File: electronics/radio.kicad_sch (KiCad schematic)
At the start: 33 parts, among them J7 SIM_Card, J9 Conn_Coaxial_Small, Q1 Q_NMOS_GSD, SW1 SW_Push, U2 TPS22953

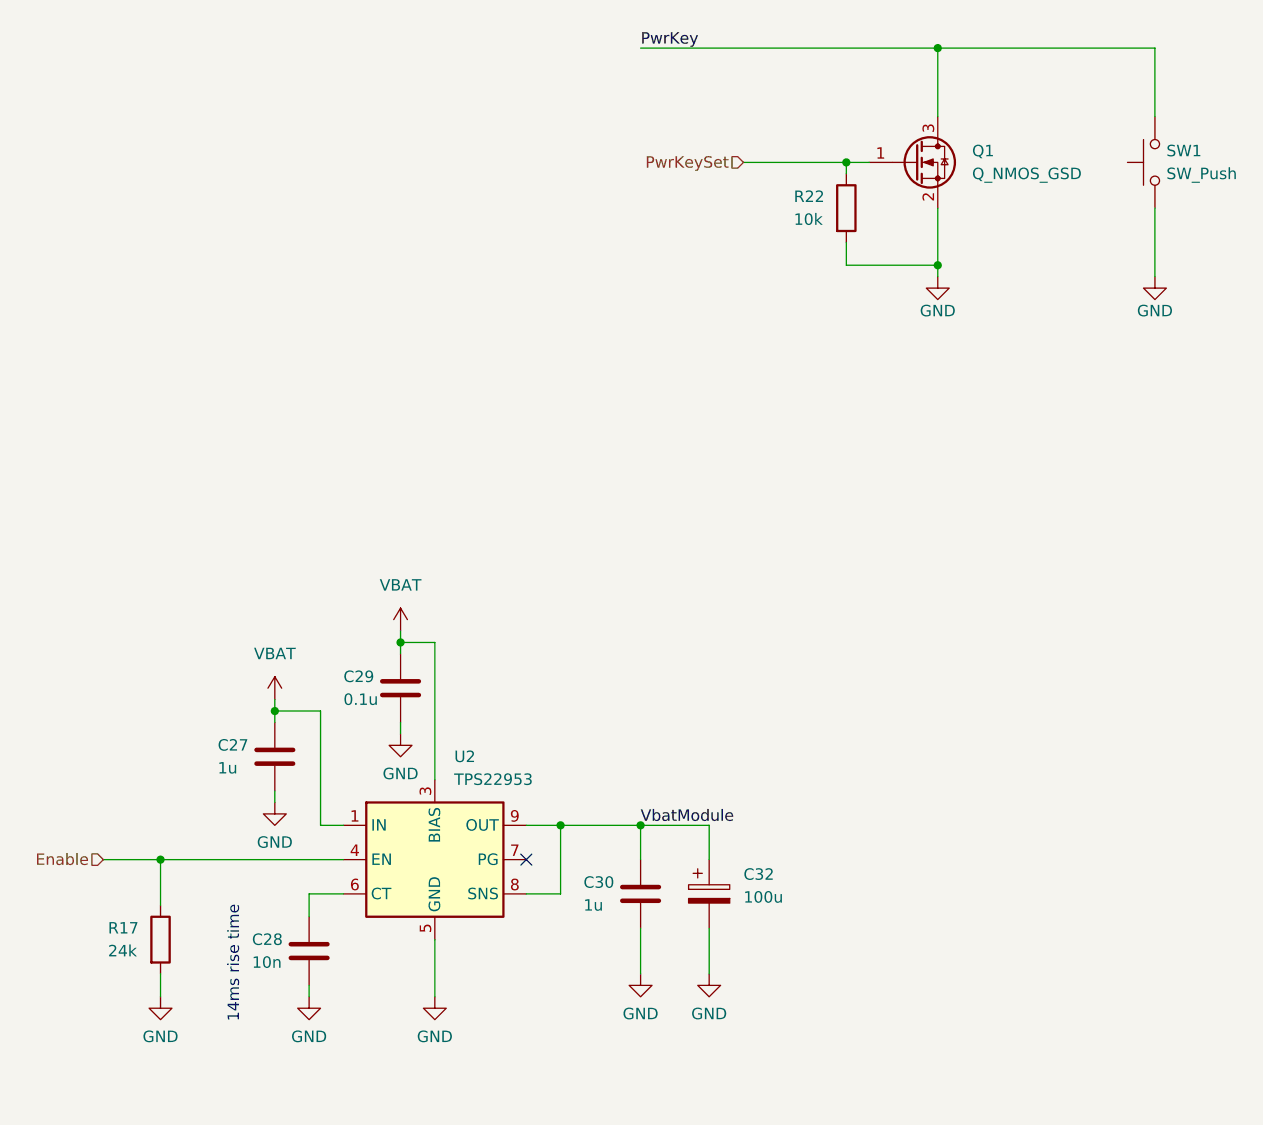
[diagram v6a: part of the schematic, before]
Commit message: electronics: add MPNs
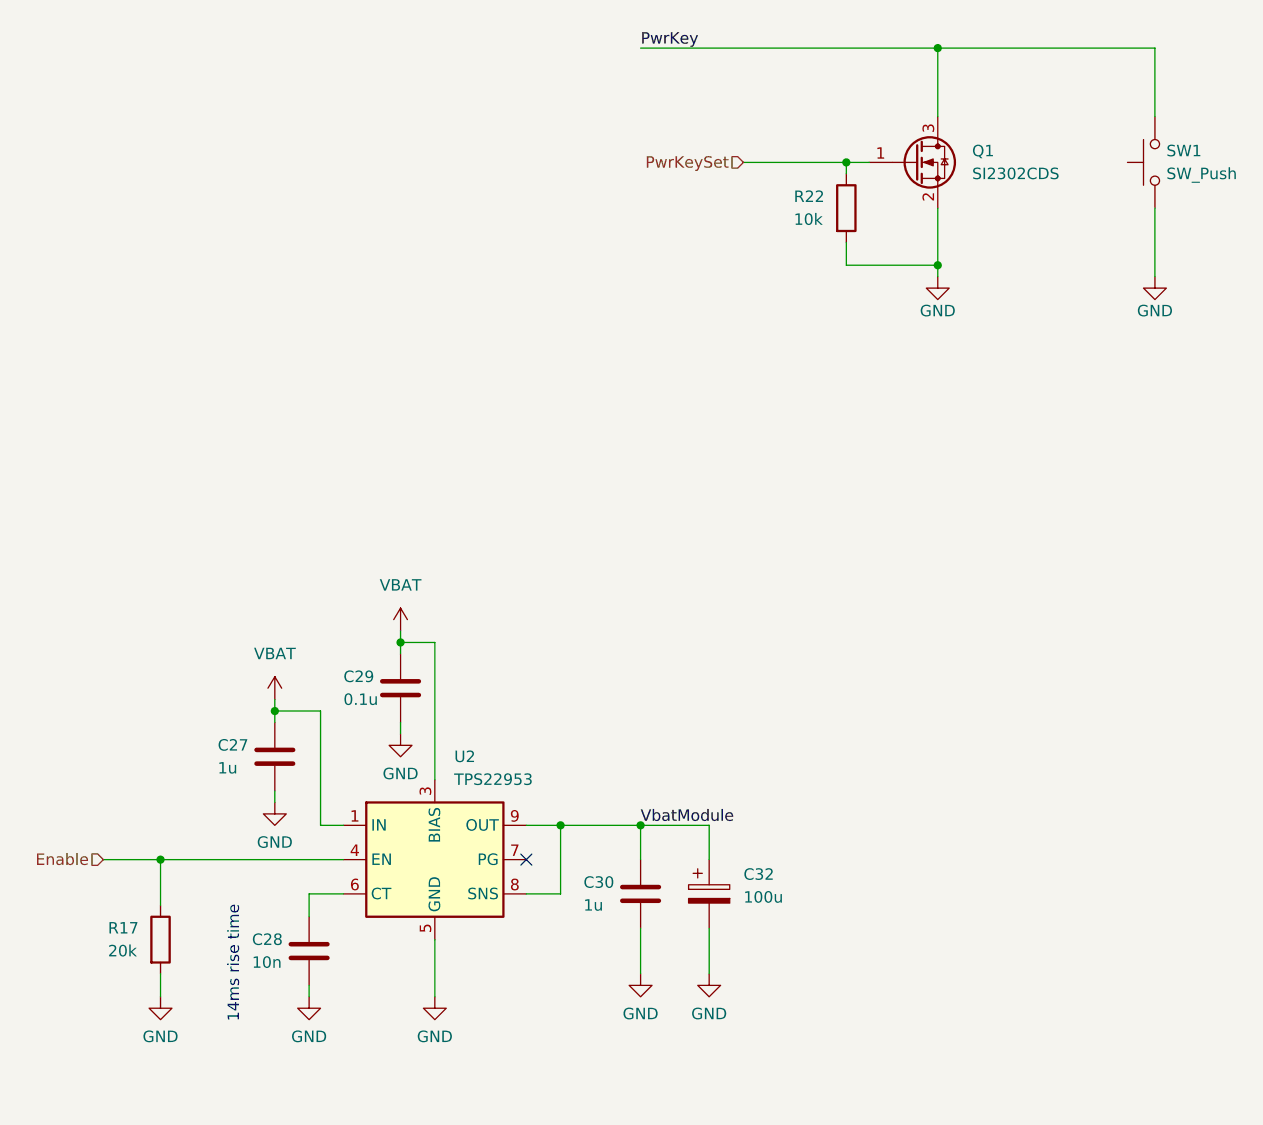
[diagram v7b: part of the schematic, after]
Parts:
- J7: MPN (none) -> NSIM-2-C
- Q1: value Q_NMOS_GSD -> SI2302CDS; MPN (none) -> SI2302CDS-T1-GE3
- R17: value 24k -> 20k
- SW1: MPN (none) -> TL3305AF160QG
- U4: MPN (none) -> A7670E-LASE
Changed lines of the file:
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@@
+			)
+		)
+		(property "MPN" "NSIM-2-C"
+			(at 259.08 92.71 0)
+			(hide yes)
+			(show_name no)
+			(do_not_autoplace no)
+			(effects
+				(font
+					(size 1.27 1.27)
+				)
 			)
 		)
@@
 			)
 		)
-		(property "Value" "24k"
+		(property "Value" "20k"
 			(at -70.612 189.23 0)
 			(show_name no)
@@
 			)
 		)
+		(property "MPN" "A7670E-LASE"
+			(at 124.46 123.19 0)
+			(hide yes)
+			(show_name no)
+			(do_not_autoplace no)
+			(effects
+				(font
+					(size 1.27 1.27)
+				)
+			)
+		)
 		(pin "87"
 		)
@@
 			)
 		)
-		(property "Value" "Q_NMOS_GSD"
+		(property "Value" "SI2302CDS"
 			(at 25.4 102.8699 0)
 			(show_name no)
@@
 		)
 		(property "Description" "N-MOSFET transistor, gate/source/drain"
+			(at 19.05 101.6 0)
+			(hide yes)
+			(show_name no)
+			(do_not_autoplace no)
+			(effects
+				(font
+					(size 1.27 1.27)
+				)
+			)
+		)
+		(property "MPN" "SI2302CDS-T1-GE3"
 			(at 19.05 101.6 0)
 			(hide yes)
@@
 			(hide yes)
 			(show_name no)
+			(do_not_autoplace no)
+			(effects
+				(font
+					(size 1.27 1.27)
+				)
+			)
+		)
+		(property "MPN" "TL3305AF160QG"
+			(at 45.72 101.6 90)
+			(hide yes)
+			(show_name no)

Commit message: electronics: simplify BOM and fix issues
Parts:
- added R15: 0R, Resistor_SMD:R_1206_3216Metric, symbol Device:R
- C24: value 10p -> 6.8p
- C27, C28, C29, C30: footprint Capacitor_SMD:C_0402_1005Metric -> Capacitor_SMD:C_0603_1608Metric
- C8: value 33p -> 22p
- R16: value 51R -> 22R
- R17: value 20k -> 10k; footprint Resistor_SMD:R_0402_1005Metric -> Resistor_SMD:R_0603_1608Metric
- R22, R26: footprint Resistor_SMD:R_0402_1005Metric -> Resistor_SMD:R_0603_1608Metric
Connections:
- net VBAT: now also R15.1
- net VbatModule: now also R15.2
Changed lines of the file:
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@@
 	(wire
 		(pts
+			(xy -46.99 138.43) (xy -40.64 138.43)
+		)
+		(stroke
+			(width 0)
+			(type default)
+		)
+	)
+	(wire
+		(pts
 			(xy 227.33 96.52) (xy 227.33 99.06)
 		)
@@
 	(wire
 		(pts
+			(xy -33.02 138.43) (xy -13.97 138.43)
+		)
+		(stroke
+			(width 0)
+			(type default)
+		)
+	)
+	(wire
+		(pts
 			(xy 54.61 62.23) (xy 66.04 62.23)
 		)
@@
 	(wire
 		(pts
+			(xy -46.99 133.35) (xy -46.99 138.43)
+		)
+		(stroke
+			(width 0)
+			(type default)
+		)
+	)
+	(wire
+		(pts
 			(xy 275.59 21.59) (xy 270.51 21.59)
 		)
@@
 		)
 	)
+	(label "VbatModule"
+		(at -13.97 138.43 180)
+		(effects
+			(font
+				(size 1.27 1.27)
+			)
+			(justify right bottom)
+		)
+	)
 	(label "SimDet"
 		(at 233.68 101.6 0)
@@
 			)
 		)
-		(property "Footprint" "Resistor_SMD:R_0402_1005Metric"
+		(property "Footprint" "Resistor_SMD:R_0603_1608Metric"
 			(at 9.652 106.68 90)
 			(hide yes)
@@
 			)
 		)
-		(property "Footprint" "Resistor_SMD:R_0402_1005Metric"
+		(property "Footprint" "Resistor_SMD:R_0603_1608Metric"
 			(at 23.622 30.48 90)
 			(hide yes)
@@
 			)
 		)
-		(property "Value" "33p"
+		(property "Value" "22p"
 			(at 46.99 69.8499 0)
 			(show_name no)
@@
 	)
 	(symbol
+		(lib_id "MyScale:VBAT")
+		(at -46.99 133.35 0)
+		(unit 1)
+		(body_style 1)
+		(exclude_from_sim no)
+		(in_bom yes)
+		(on_board yes)
+		(in_pos_files yes)
+		(dnp no)
+		(fields_autoplaced yes)
+		(property "Reference" "#PWR0100"
+			(at -46.99 137.16 0)
+			(hide yes)
+			(show_name no)
+			(do_not_autoplace no)
+			(effects
+				(font
+					(size 1.27 1.27)
+				)
+			)
+		)
+		(property "Value" "VBAT"
+			(at -46.99 128.27 0)
+			(show_name no)
+			(do_not_autoplace no)
+			(effects
+				(font
+					(size 1.27 1.27)
+				)
+			)
+		)
+		(property "Footprint" ""
+			(at -46.99 133.35 0)
+			(hide yes)
+			(show_name no)
+			(do_not_autoplace no)
+			(effects
+				(font
+					(size 1.27 1.27)
+				)
+			)
+		)
+		(property "Datasheet" ""
+			(at -46.99 133.35 0)
+			(hide yes)
+			(show_name no)
+			(do_not_autoplace no)
+			(effects
+				(font
+					(size 1.27 1.27)
+				)
+			)
+		)
+		(property "Description" "Power symbol creates a global label with name \"VBAT\""
+			(at -46.99 133.35 0)
+			(hide yes)
+			(show_name no)
+			(do_not_autoplace no)
+			(effects
+				(font
+					(size 1.27 1.27)
+				)
+			)
+		)
+		(pin "1"
+		)
+		(instances
+			(project "MyScale"
+				(path "/b5eed584-7820-40e8-871b-2aa5dd8c83ec/d79f2b7f-8f6c-4118-9551-ed509f2ef890"
+					(reference "#PWR0100")
+					(unit 1)
+				)
+			)
+		)
+	)
+	(symbol
 		(lib_id "Device:C")
 		(at 77.47 68.58 0)
@@
 			)
 		)
-		(property "Value" "20k"
+		(property "Value" "10k"
 			(at -70.612 189.23 0)
 			(show_name no)
@@
 			)
 		)
-		(property "Footprint" "Resistor_SMD:R_0402_1005Metric"
+		(property "Footprint" "Resistor_SMD:R_0603_1608Metric"
 			(at -66.548 187.96 90)
 			(hide yes)
@@
 			)
 		)
-		(property "Value" "10p"
+		(property "Value" "6.8p"
 			(at 58.42 69.8499 0)
 			(show_name no)
@@
 			)
 		)
-		(property "Value" "51R"
+		(property "Value" "22R"
 			(at 180.34 143.5099 0)
 			(show_name no)
@@
 			)
 		)
-		(property "Footprint" "Capacitor_SMD:C_0402_1005Metric"
+		(property "Footprint" "Capacitor_SMD:C_0603_1608Metric"
 			(at -47.2948 193.04 0)
 			(hide yes)
@@
 			)
 		)
-		(property "Footprint" "Capacitor_SMD:C_0402_1005Metric"
+		(property "Footprint" "Capacitor_SMD:C_0603_1608Metric"
 			(at -51.1048 171.45 0)
 			(hide yes)
@@
 	)
 	(symbol
+		(lib_id "Device:R")
+		(at -36.83 138.43 90)
+		(unit 1)
+		(body_style 1)
+		(exclude_from_sim no)
+		(in_bom no)
+		(on_board yes)
+		(in_pos_files no)
+		(dnp yes)
+		(fields_autoplaced yes)
+		(property "Reference" "R15"
+			(at -36.83 132.08 90)
+			(show_name no)
+			(do_not_autoplace no)
+			(effects
+				(font
+					(size 1.27 1.27)
+				)
+			)
+		)
+		(property "Value" "0R"
+			(at -36.83 134.62 90)
+			(show_name no)
+			(do_not_autoplace no)
+			(effects
+				(font
+					(size 1.27 1.27)
+				)
+			)
+		)
+		(property "Footprint" "Resistor_SMD:R_1206_3216Metric"
+			(at -36.83 140.208 90)
+			(hide yes)
+			(show_name no)
+			(do_not_autoplace no)
+			(effects
+				(font
+					(size 1.27 1.27)
+				)
+			)
+		)
+		(property "Datasheet" ""
+			(at -36.83 138.43 0)
+			(hide yes)
+			(show_name no)
+			(do_not_autoplace no)
+			(effects
+				(font
+					(size 1.27 1.27)
+				)
+			)
+		)
+		(property "Description" "Resistor"
+			(at -36.83 138.43 0)
+			(hide yes)
+			(show_name no)
+			(do_not_autoplace no)
+			(effects
+				(font
+					(size 1.27 1.27)
+				)
+			)
+		)
+		(pin "1"
+		)
+		(pin "2"
+		)
+		(instances
+			(project "MyScale"
+				(path "/b5eed584-7820-40e8-871b-2aa5dd8c83ec/d79f2b7f-8f6c-4118-9551-ed509f2ef890"
+					(reference "R15")
+					(unit 1)
+				)
+			)
+		)
+	)
+	(symbol
 		(lib_id "power:GND")
 		(at 238.76 34.29 0)
@@
 			)
 		)
-		(property "Footprint" "Capacitor_SMD:C_0402_1005Metric"
+		(property "Footprint" "Capacitor_SMD:C_0603_1608Metric"
 			(at -10.4648 186.69 0)
 			(hide yes)
@@
 			)
 		)
-		(property "Footprint" "Capacitor_SMD:C_0402_1005Metric"
+		(property "Footprint" "Capacitor_SMD:C_0603_1608Metric"
 			(at -37.1348 163.83 0)
 			(hide yes)
